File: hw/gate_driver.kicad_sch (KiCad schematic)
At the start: 9 parts, among them U501 LMG1210RVRT

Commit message: Added proper signal TPs for Vsw, both gate signals, and PWM, added BNC connector for PWM control signal to STM analog pin, increased Vsw zone on F.cu, in.1, and in.2, reduced vias directly under fets, changed heatsink holesto pads for proper zone margins
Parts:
- added TP302: Gate 1 Test Point, mppt:SignalTP, symbol Connector:TestPoint_2Pole
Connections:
- net SW2_OUT: now also TP302.1
- net V_SW: now also TP302.2
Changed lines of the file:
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@@
   (junction (at 181.61 78.74) (diameter 0) (color 0 0 0 0)
   )
+  (junction (at 186.69 99.06) (diameter 0) (color 0 0 0 0)
+  )
   (junction (at 110.49 78.74) (diameter 0) (color 0 0 0 0)
   )
   (no_connect (at 138.43 109.22))
+  (wire (pts (xy 184.15 99.06) (xy 186.69 99.06))
+    (stroke (width 0) (type default))
+  )
   (wire (pts (xy 173.99 99.06) (xy 179.07 99.06))
     (stroke (width 0) (type default))
@@
     (stroke (width 0) (type default))
   )
+  (wire (pts (xy 186.69 99.06) (xy 187.325 99.06))
+    (stroke (width 0) (type default))
+  )
   (wire (pts (xy 129.54 66.04) (xy 129.54 101.6))
     (stroke (width 0) (type default))
@@
     (stroke (width 0) (type default))
   )
+  (wire (pts (xy 186.69 99.06) (xy 186.69 100.965))
+    (stroke (width 0) (type default))
+  )
   (text "Reselect after redeterming deadtime." (at 90.17 107.95 0)
     (effects (font (size 1.27 1.27)) (justify left bottom))
@@
     (effects (font (size 1.27 1.27)) (justify left bottom))
   )
-  (hierarchical_label "SW2_OUT" (shape input) (at 184.15 99.06 0) (fields_autoplaced)
+  (hierarchical_label "SW2_OUT" (shape input) (at 187.325 99.06 0) (fields_autoplaced)
     (effects (font (size 1.27 1.27)) (justify left))
   )
@@
   )
   (hierarchical_label "SW1_OUT" (shape input) (at 184.15 93.98 0) (fields_autoplaced)
+    (effects (font (size 1.27 1.27)) (justify left))
+  )
+  (hierarchical_label "V_SW" (shape input) (at 186.69 111.125 0) (fields_autoplaced)
     (effects (font (size 1.27 1.27)) (justify left))
   )
@@
         )
       )
+    )
+  )
+  (symbol (lib_id "Connector:TestPoint_2Pole") (at 186.69 106.045 270) (unit 1)
+    (in_bom yes) (on_board yes) (dnp no) (fields_autoplaced)
+    (property "Reference" "TP302" (at 189.23 105.41 90)
+      (effects (font (size 1.27 1.27)) (justify left))
+    )
+    (property "Value" "Gate 1 Test Point" (at 189.23 107.95 90)
+      (effects (font (size 1.27 1.27)) (justify left))
+    )
+    (property "Footprint" "mppt:SignalTP" (at 186.69 106.045 0)
+      (effects (font (size 1.27 1.27)) hide)
+    )
+    (property "Datasheet" "~" (at 186.69 106.045 0)
+      (effects (font (size 1.27 1.27)) hide)
+    )
+    (pin "1")
+    (pin "2")
+    (instances
+      (project "mppt"
+        (path "/06fd3a42-664d-41bc-bf0f-b5ee0ddcc902/9cd55a57-0ec8-481d-b571-b5fdbe353ce7"
+          (reference "TP302") (unit 1)
+        )
+        (path "/06fd3a42-664d-41bc-bf0f-b5ee0ddcc902/d2872b58-d342-47d2-86ca-67a04f8e2122"
+          (reference "TP1") (unit 1)
+        )
+      )

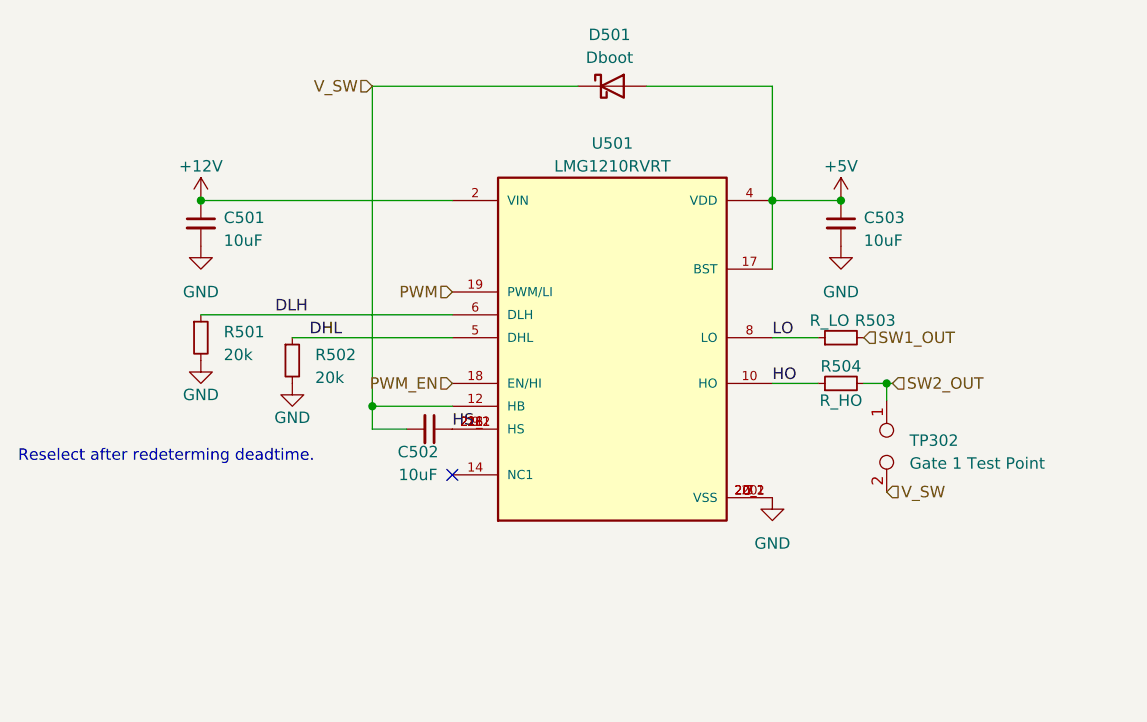
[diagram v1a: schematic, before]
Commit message: rebuild schematic, passes ERC, bom completed
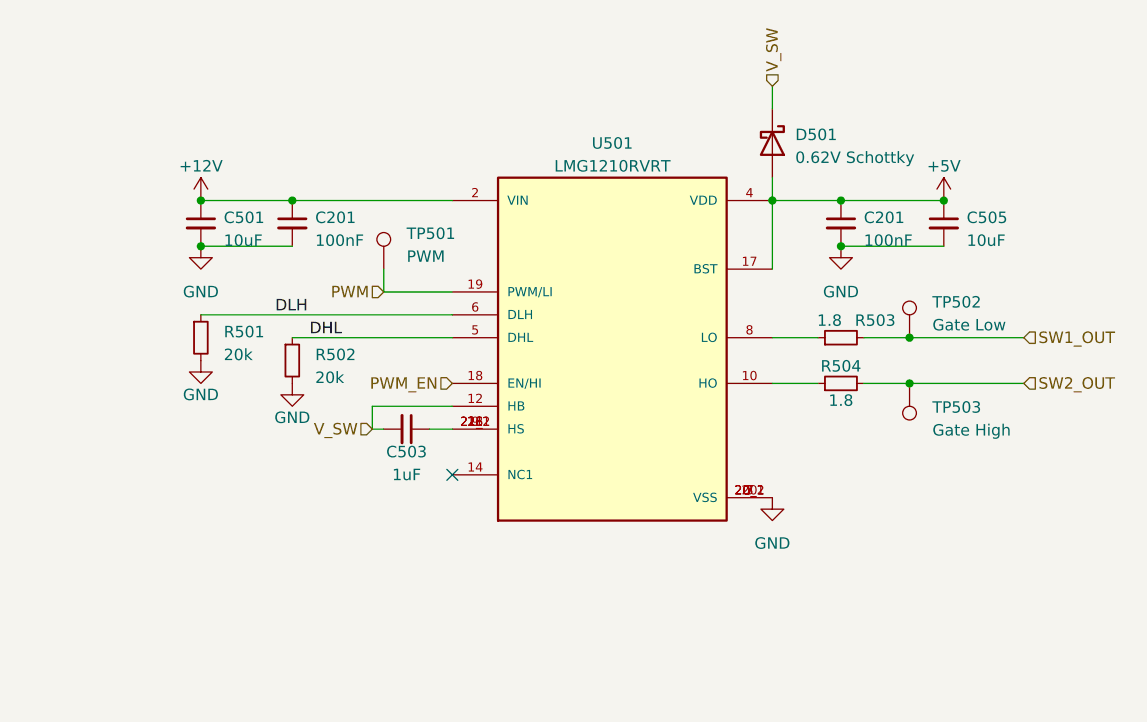
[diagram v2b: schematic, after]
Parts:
- removed TP302: Gate 1 Test Point, mppt:SignalTP, symbol Connector:TestPoint_2Pole
- added C201 (x2): 100nF, Capacitor_SMD:C_0402_1005Metric, symbol Device:C_Small
- added TP501: PWM, TestPoint:TestPoint_Keystone_5000-5004_Miniature, symbol Connector:TestPoint
- added TP502: Gate Low, TestPoint:TestPoint_Keystone_5000-5004_Miniature, symbol Connector:TestPoint
- added TP503: Gate High, TestPoint:TestPoint_Keystone_5000-5004_Miniature, symbol Connector:TestPoint
- C501: footprint Capacitor_SMD:C_0402_1005Metric -> Capacitor_SMD:C_0603_1608Metric; Distributor (none) -> JLCPCB; In Stock? Y -> (none); JLC P/N (none) -> C96446; Manufacturer (none) -> Samsung Electro-Mechanics; Mfg PN CL10A226MO7JZNC -> (none); P/N (none) -> CL10A106MA8NRNC; Projected Cost 0.61 -> (none)
- C503: renamed from C502; value 10uF -> 1uF; Distributor (none) -> JLCPCB; In Stock? Y -> (none); JLC P/N (none) -> C52923; Manufacturer (none) -> Samsung Electro-Mechanics; Mfr PN GRM158R61A226ME15D -> (none); P/N (none) -> CL05A105KA5NQNC; Projected Cost 0.48 -> (none)
- C505: renamed from C503; footprint Capacitor_SMD:C_0402_1005Metric -> Capacitor_SMD:C_0603_1608Metric; Distributor (none) -> JLCPCB; In Stock? Y -> (none); JLC P/N (none) -> C96446; Manufacturer (none) -> Samsung Electro-Mechanics; Mfr PN GRM158R61A226ME15D -> (none); P/N (none) -> CL10A106MA8NRNC; Projected Cost 0.48 -> (none)
- D501: value Dboot -> 0.62V Schottky; footprint Diode_SMD:D_SOD-323 -> mppt:SODFL5226X110N; Distributor (none) -> Mouser; In Stock? Y -> (none); Manufacturer (none) -> STMicroelectronics; Mfg PN BAS3010A03WE6327HTSA1 -> (none); P/N (none) -> 511-STPS1170AF; Projected Cost 0.51 -> (none)
- R501, R502: Distributor (none) -> JLCPCB; JLC P/N (none) -> C25765; Manufacturer (none) -> Uniroyal Elec; P/N (none) -> 0402WGF2002TCE
- R503: value R_LO -> 1.8; Distributor (none) -> JLCPCB; JLC P/N (none) -> C423254; Manufacturer (none) -> Uniroyal Elec; P/N (none) -> 0402WGF118KTCE
- R504: value R_HO -> 1.8; Distributor (none) -> JLCPCB; JLC P/N (none) -> C423254; Manufacturer (none) -> Uniroyal Elec; P/N (none) -> 0402WGF118KTCE
- U501: Distributor (none) -> TI; In Stock? Y -> (none); MANUFACTURER Texas Instruments -> (none); MAXIMUM_PACKAGE_HEIGHT 0.8mm -> (none); Manufacturer (none) -> TI; P/N (none) -> LMG1210RVRR; PARTREV D -> (none); Projected Cost 4.10 -> (none); STANDARD Manufacturer Recommendations -> (none)
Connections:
- net +12V: now also C201.1
- net +5V: now also C201.1
- net GND: now also C201.2, C201.2
- net PWM: now also TP501.1
- net SW1_OUT: now also TP502.1
- net SW2_OUT: now also TP503.1
- net HO: no longer names the net of R504.1, U501.10 (HO)
- net HS: no longer names the net of C503.1, U501.13 (HS), U501.16 (HS), U501.21 (HS), U501.21_1 (HS), U501.21_2 (HS), U501.9 (HS)
- net LO: no longer names the net of R503.1, U501.8 (LO)
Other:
- note removed: "Reselect after redeterming deadtime."
- moved on the sheet: C503, C505, D501

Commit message: savestate layout
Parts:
- removed TP501: PWM, TestPoint:TestPoint_Keystone_5000-5004_Miniature, symbol Connector:TestPoint
- removed TP502: Gate Low, TestPoint:TestPoint_Keystone_5000-5004_Miniature, symbol Connector:TestPoint
- removed TP503: Gate High, TestPoint:TestPoint_Keystone_5000-5004_Miniature, symbol Connector:TestPoint
- added TP501, TP502, TP503: TestPoint_2Pole, mppt:SignalTP, symbol Connector:TestPoint_2Pole
- U501: footprint IC_LMG1210RVRT -> mppt:IC_LMG1210RVRT
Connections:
- net GND: now also TP501.2, TP502.2, TP503.2
- net PWM: now also TP501.1
- net SW1_OUT: now also TP502.1
- net SW2_OUT: now also TP503.1

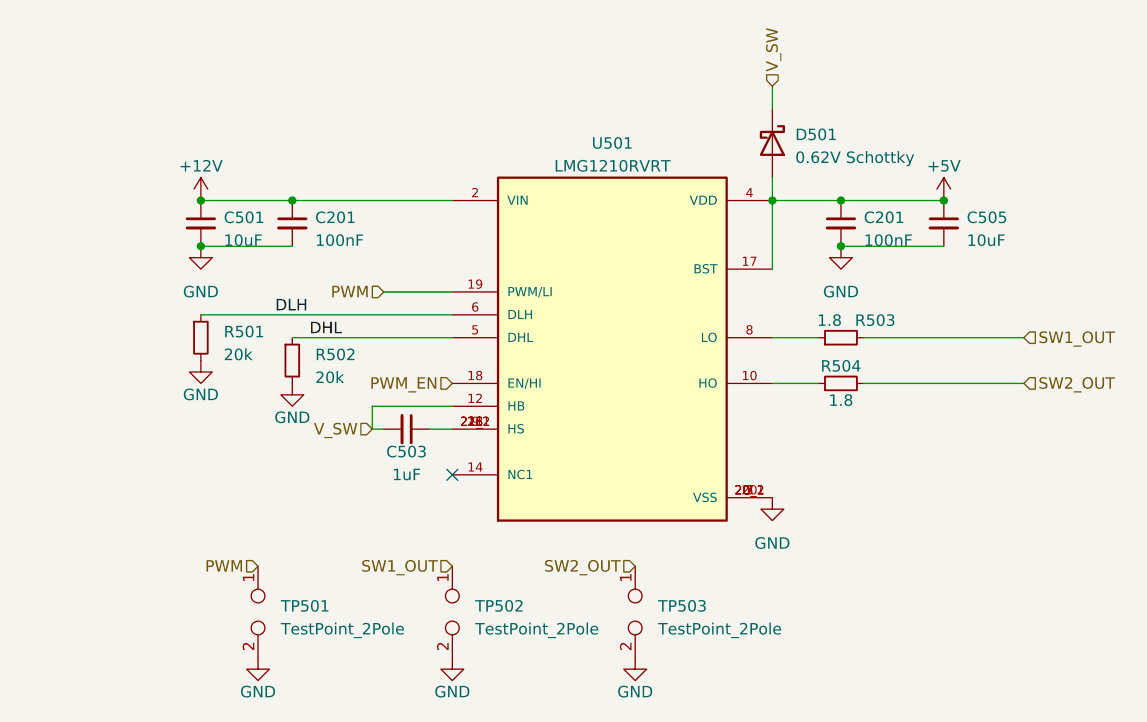
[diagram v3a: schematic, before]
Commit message: production files for v0.1.0. Change cap power calc to be based off i_rms of i_pkpk, not i_pk + r_l_a
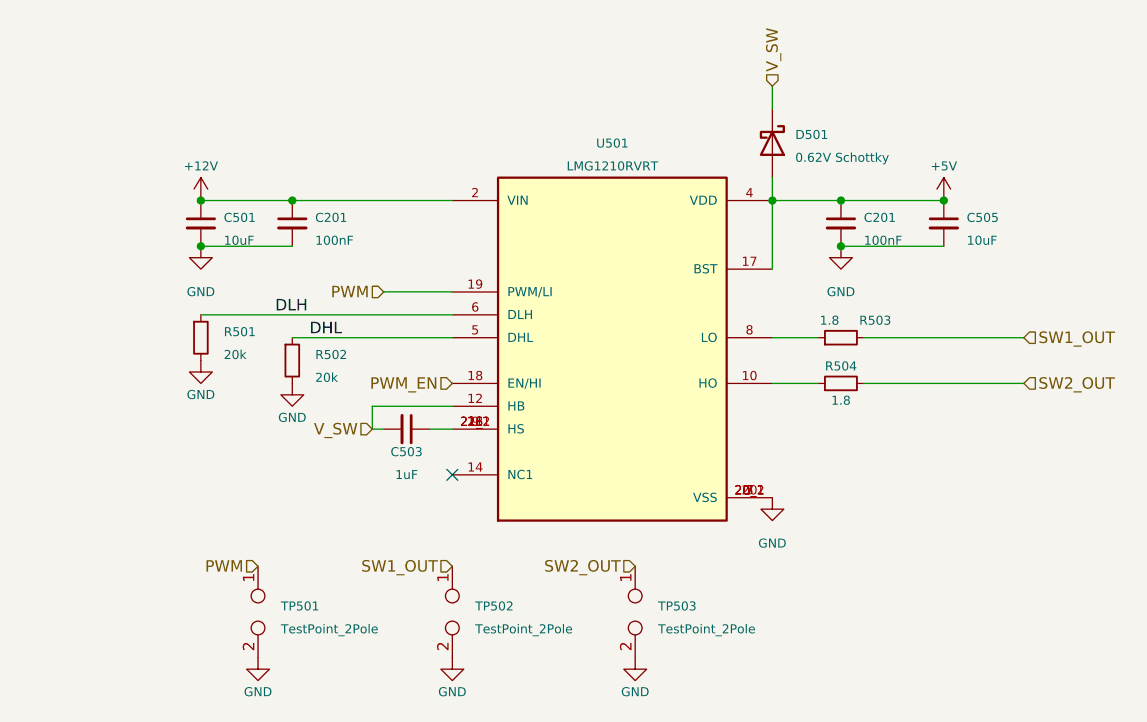
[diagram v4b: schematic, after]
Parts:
- C201: LCSC Part # (none) -> C307331
- C501, C505: LCSC Part # (none) -> C96446
- C503: LCSC Part # (none) -> C52923
- R501, R502: LCSC Part # (none) -> C25765
- R503, R504: LCSC Part # (none) -> C423254
- U501: Distributor TI -> Texas Instruments; Manufacturer TI -> Texas Instruments

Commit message: fixed gate driver circuit, filleted filled zones, ensured DRC conformity regarding clearances
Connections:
- net +5V: no longer D501.2 (A), U501.17 (BST)
- net V_SW: now also C503.1, U501.13 (HS), U501.16 (HS), U501.21 (HS), U501.21_1 (HS), U501.21_2 (HS), U501.9 (HS); no longer C503.2, D501.1 (K), U501.12 (HB)
- net HO: now reaches R504.1, U501.10 (HO)
- net LO: now reaches R503.1, U501.8 (LO)
- new net BST: D501.2 (A), U501.17 (BST)
- new net HB: C503.2, D501.1 (K), U501.12 (HB)
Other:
- moved on the sheet: C201, C503, C505, D501, R501, R502
